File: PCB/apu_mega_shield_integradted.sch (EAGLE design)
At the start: 79 parts, among them IC1 74AHC573, IC10 DAC, IC11 IS62C1024AL, IC2 4050D, IC3 DS1307, IC4 LP298XS, IC5 S-SMP, IC6 S-DSP, IC7 LM2904, IC8 5x832 SRAM, IC9 5x832 SRAM, Q1 32.768, X1 MICROSDMOLEX

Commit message: R1 removed from PCB. It was supposed to be the current limiting resistor for the LCD backlight, however, the LCD module in use already has a current limiting resistor mounted right on that module.
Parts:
- removed R1: 220, resistor:R-US_R0805
- C10, C13: value (none) -> 100pF
- C11, C14: value (none) -> 1800pF
- C12, C9: value (none) -> 1000pF
- C15, C16, C17, C18, C19, C22, C23: value (none) -> 0.1uF
- C20, C21: value (none) -> 3pF
- C50, C51: value (none) -> 47uF
- DOWN: value (none) -> DOWN
- LEFT: value (none) -> LEFT
- R16, R17, R18, R19, R20, R21: value (none) -> 22K
- R22, R23: value (none) -> 5.1K
- RIGHT: value (none) -> RIGHT
- SELECT: value (none) -> SELECT
- UP: value (none) -> UP
- X2: value (none) -> 24.576Mhz
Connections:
- removed net !MUTE: IC6.!MUTE
- removed net SMPCLK: IC6.SMPCLK
- net N$14: now also U$6.46; no longer R1.2
- net VCC: no longer R1.1
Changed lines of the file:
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@@
 <part name="GND1" library="supply1" deviceset="GND" device=""/>
 <part name="JP1" library="pinhead" deviceset="PINHD-1X16" device="" value="LCD"/>
-<part name="UP" library="switch-omron" deviceset="10-XX" device=""/>
-<part name="DOWN" library="switch-omron" deviceset="10-XX" device=""/>
-<part name="LEFT" library="switch-omron" deviceset="10-XX" device=""/>
-<part name="RIGHT" library="switch-omron" deviceset="10-XX" device=""/>
-<part name="SELECT" library="switch-omron" deviceset="10-XX" device=""/>
+<part name="UP" library="switch-omron" deviceset="10-XX" device="" value="UP"/>
+<part name="DOWN" library="switch-omron" deviceset="10-XX" device="" value="DOWN"/>
+<part name="LEFT" library="switch-omron" deviceset="10-XX" device="" value="LEFT"/>
+<part name="RIGHT" library="switch-omron" deviceset="10-XX" device="" value="RIGHT"/>
+<part name="SELECT" library="switch-omron" deviceset="10-XX" device="" value="SELECT"/>
 <part name="Q1" library="crystal" deviceset="CRYTAL" device="SMD" value="32.768"/>
 <part name="IC3" library="adafruit" deviceset="DS1307" device="SMT" value="DS1307"/>
@@
 <part name="SUPPLY2" library="supply2" deviceset="GND" device=""/>
 <part name="X1" library="adafruit" deviceset="MICROSD" device="MOLEX"/>
-<part name="R1" library="resistor" deviceset="R-US_" device="R0805" value="220"/>
 <part name="R2" library="resistor" deviceset="R-US_" device="R0805" value="10K"/>
 <part name="R3" library="resistor" deviceset="R-US_" device="R0805" value="10K"/>
@@
 <part name="R15" library="resistor" deviceset="R-US_" device="R0805" value="10K"/>
 <part name="IC5" library="apu_pcb" deviceset="S-SMP" device=""/>
-<part name="C50" library="apu_pcb" deviceset="CAPACITOR" device=""/>
-<part name="C51" library="apu_pcb" deviceset="CAPACITOR" device=""/>
+<part name="C50" library="apu_pcb" deviceset="CAPACITOR" device="" value="47uF"/>
+<part name="C51" library="apu_pcb" deviceset="CAPACITOR" device="" value="47uF"/>
 <part name="IC6" library="apu_pcb" deviceset="S-DSP" device=""/>
 <part name="P+4" library="supply1" deviceset="VCC" device=""/>
 <part name="GND3" library="supply1" deviceset="GND" device=""/>
-<part name="C9" library="apu_pcb" deviceset="C0805" device=""/>
-<part name="C10" library="apu_pcb" deviceset="C0805" device=""/>
-<part name="C11" library="apu_pcb" deviceset="C0805" device=""/>
-<part name="C12" library="apu_pcb" deviceset="C0805" device=""/>
-<part name="C13" library="apu_pcb" deviceset="C0805" device=""/>
-<part name="C14" library="apu_pcb" deviceset="C0805" device=""/>
-<part name="C15" library="apu_pcb" deviceset="C0805" device=""/>
-<part name="C16" library="apu_pcb" deviceset="C0805" device=""/>
-<part name="C17" library="apu_pcb" deviceset="C0805" device=""/>
-<part name="C18" library="apu_pcb" deviceset="C0805" device=""/>
-<part name="C19" library="apu_pcb" deviceset="C0805" device=""/>
-<part name="C20" library="apu_pcb" deviceset="C0805" device=""/>
-<part name="C21" library="apu_pcb" deviceset="C0805" device=""/>
-<part name="R16" library="apu_pcb" deviceset="R0805" device=""/>
-<part name="R17" library="apu_pcb" deviceset="R0805" device=""/>
-<part name="R18" library="apu_pcb" deviceset="R0805" device=""/>
-<part name="R19" library="apu_pcb" deviceset="R0805" device=""/>
-<part name="R20" library="apu_pcb" deviceset="R0805" device=""/>
-<part name="R21" library="apu_pcb" deviceset="R0805" device=""/>
-<part name="R22" library="apu_pcb" deviceset="R0805" device=""/>
-<part name="R23" library="apu_pcb" deviceset="R0805" device=""/>
-<part name="C22" library="apu_pcb" deviceset="C0805" device=""/>
+<part name="C9" library="apu_pcb" deviceset="C0805" device="" value="1000pF"/>
+<part name="C10" library="apu_pcb" deviceset="C0805" device="" value="100pF"/>
+<part name="C11" library="apu_pcb" deviceset="C0805" device="" value="1800pF"/>
+<part name="C12" library="apu_pcb" deviceset="C0805" device="" value="1000pF"/>
+<part name="C13" library="apu_pcb" deviceset="C0805" device="" value="100pF"/>
+<part name="C14" library="apu_pcb" deviceset="C0805" device="" value="1800pF"/>
+<part name="C15" library="apu_pcb" deviceset="C0805" device="" value="0.1uF"/>
+<part name="C16" library="apu_pcb" deviceset="C0805" device="" value="0.1uF"/>
+<part name="C17" library="apu_pcb" deviceset="C0805" device="" value="0.1uF"/>
+<part name="C18" library="apu_pcb" deviceset="C0805" device="" value="0.1uF"/>
+<part name="C19" library="apu_pcb" deviceset="C0805" device="" value="0.1uF"/>
+<part name="C20" library="apu_pcb" deviceset="C0805" device="" value="3pF"/>
+<part name="C21" library="apu_pcb" deviceset="C0805" device="" value="3pF"/>
+<part name="R16" library="apu_pcb" deviceset="R0805" device="" value="22K"/>
+<part name="R17" library="apu_pcb" deviceset="R0805" device="" value="22K"/>
+<part name="R18" library="apu_pcb" deviceset="R0805" device="" value="22K"/>
+<part name="R19" library="apu_pcb" deviceset="R0805" device="" value="22K"/>
+<part name="R20" library="apu_pcb" deviceset="R0805" device="" value="22K"/>
+<part name="R21" library="apu_pcb" deviceset="R0805" device="" value="22K"/>
+<part name="R22" library="apu_pcb" deviceset="R0805" device="" value="5.1K"/>
+<part name="R23" library="apu_pcb" deviceset="R0805" device="" value="5.1K"/>
+<part name="C22" library="apu_pcb" deviceset="C0805" device="" value="0.1uF"/>
 <part name="GND5" library="supply1" deviceset="GND" device=""/>
 <part name="GND6" library="supply1" deviceset="GND" device=""/>
@@
 <part name="IC8" library="apu_pcb" deviceset="SRAM" device="" value="5x832 SRAM"/>
 <part name="IC9" library="apu_pcb" deviceset="SRAM" device="" value="5x832 SRAM"/>
-<part name="X2" library="apu_pcb" deviceset="CRYSTAL" device=""/>
+<part name="X2" library="apu_pcb" deviceset="CRYSTAL" device="" value="24.576Mhz"/>
 <part name="IC10" library="apu_pcb" deviceset="UPD6376" device="" value="DAC"/>
-<part name="C23" library="apu_pcb" deviceset="C0805" device=""/>
+<part name="C23" library="apu_pcb" deviceset="C0805" device="" value="0.1uF"/>
 <part name="C24" library="rcl" deviceset="C-EU" device="C0805" value="0.1uF"/>
 <part name="P+5" library="supply1" deviceset="VCC" device=""/>
@@
 <instance part="UP" gate="1" x="147.32" y="-17.78" smashed="yes" rot="MR270">
 <attribute name="NAME" x="148.844" y="-22.606" size="1.778" layer="95" rot="MR0"/>
-<attribute name="VALUE" x="144.145" y="-13.97" size="1.778" layer="96" rot="MR0"/>
 </instance>
 <instance part="DOWN" gate="1" x="147.32" y="-30.48" smashed="yes" rot="MR270">
 <attribute name="NAME" x="150.876" y="-35.56" size="1.778" layer="95" rot="MR0"/>
-<attribute name="VALUE" x="144.145" y="-26.67" size="1.778" layer="96" rot="MR0"/>
 </instance>
 <instance part="LEFT" gate="1" x="132.08" y="-22.86" smashed="yes" rot="MR270">
 <attribute name="NAME" x="135.128" y="-27.94" size="1.778" layer="95" rot="MR0"/>
-<attribute name="VALUE" x="128.905" y="-19.05" size="1.778" layer="96" rot="MR0"/>
 </instance>
 <instance part="RIGHT" gate="1" x="165.1" y="-22.86" smashed="yes" rot="MR270">
 <attribute name="NAME" x="169.164" y="-27.686" size="1.778" layer="95" rot="MR0"/>
-<attribute name="VALUE" x="161.925" y="-19.05" size="1.778" layer="96" rot="MR0"/>
 </instance>
 <instance part="SELECT" gate="1" x="182.88" y="-22.86" smashed="yes" rot="MR270">
 <attribute name="NAME" x="187.198" y="-27.686" size="1.778" layer="95" rot="MR0"/>
-<attribute name="VALUE" x="179.705" y="-19.05" size="1.778" layer="96" rot="MR0"/>
 </instance>
 <instance part="Q1" gate="G$1" x="111.76" y="127" rot="R180"/>
@@
 <instance part="SUPPLY2" gate="GND" x="383.54" y="-15.24"/>
 <instance part="X1" gate="G$1" x="353.06" y="15.24"/>
-<instance part="R1" gate="G$1" x="233.68" y="121.92" rot="R270"/>
 <instance part="R2" gate="G$1" x="142.24" y="5.08" rot="R270"/>
 <instance part="R3" gate="G$1" x="182.88" y="5.08" rot="R270"/>
@@
 <wire x1="243.84" y1="114.3" x2="243.84" y2="116.84" width="0.1524" layer="91"/>
 <label x="256.54" y="134.62" size="1.778" layer="95"/>
-<pinref part="R1" gate="G$1" pin="1"/>
-<wire x1="233.68" y1="127" x2="243.84" y2="127" width="0.1524" layer="91"/>
-<junction x="243.84" y="127"/>
 </segment>
 <segment>
@@
 <segment>
 <pinref part="JP1" gate="A" pin="15"/>
-<pinref part="R1" gate="G$1" pin="2"/>
 <wire x1="233.68" y1="111.76" x2="233.68" y2="116.84" width="0.1524" layer="91"/>
+<wire x1="233.68" y1="116.84" x2="251.46" y2="116.84" width="0.1524" layer="91"/>
+<wire x1="251.46" y1="116.84" x2="251.46" y2="101.6" width="0.1524" layer="91"/>
+<pinref part="U$6" gate="G$1" pin="46"/>
+<wire x1="251.46" y1="101.6" x2="259.08" y2="101.6" width="0.1524" layer="91"/>
 </segment>
 </net>
@@
 </instances>
 <busses>
-<bus name="PA[0..7],PD[0..7],!P_RD,!P_WR,!RESET,!MUTE,SMPCLK,LEFT,RIGHT,GND,VCC,XTAL1,XTAL2,A[0..14],D[0..7],!CE0,!CE1,!OE,!WE,L.OUT,R.OUT,BCK,LRCK,SO,AVCC">
+<bus name="PA[0..7],PD[0..7],!RD,!WR,RST,!MUTE,SMPCLK,LEFT,RIGHT,GND,VCC,XTAL1,XTAL2,A[0..32],D[0..15],!CE0,!CE1,!OE,!WE,L.OUT,R.OUT,BCK,LRCK,SO,AVCC">
 <segment>
 <wire x1="134.62" y1="60.96" x2="134.62" y2="12.7" width="0.762" layer="92"/>
@@
 </segment>
 </net>
-<net name="SMPCLK" class="0">
-<segment>
-<pinref part="IC6" gate="G$1" pin="SMPCLK"/>
-<wire x1="139.7" y1="55.88" x2="134.62" y2="55.88" width="0.1524" layer="91"/>
-</segment>
-</net>
-<net name="!MUTE" class="1">
-<segment>
-<pinref part="IC6" gate="G$1" pin="!MUTE"/>
-<wire x1="139.7" y1="58.42" x2="134.62" y2="58.42" width="0.1524" layer="91"/>
-</segment>
-</net>

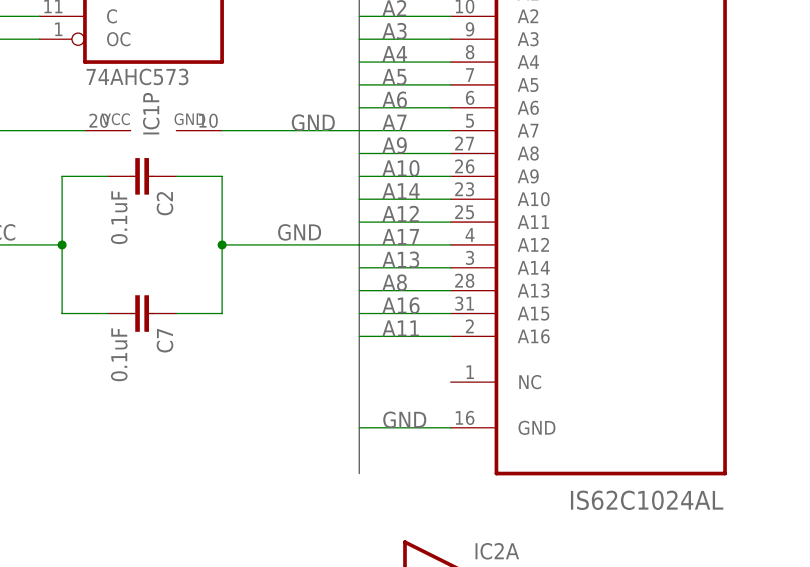
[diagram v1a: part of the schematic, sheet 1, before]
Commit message: Optimized layout a bit more.
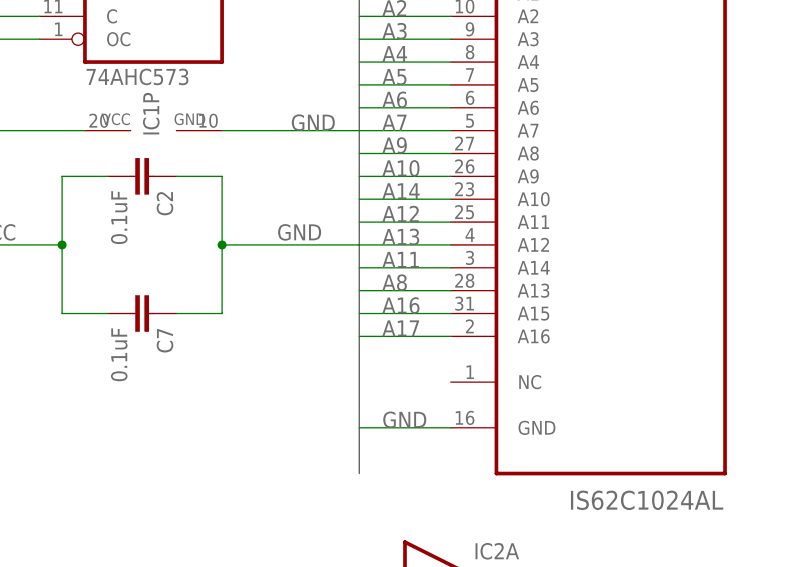
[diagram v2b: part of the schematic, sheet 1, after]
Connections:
- net A11: now also IC11.A14; no longer IC11.A16
- net A13: now also IC11.A12; no longer IC11.A14
- net A17: now also IC11.A16; no longer IC11.A12
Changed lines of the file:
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@@
 <net name="A11" class="0">
-<segment>
-<pinref part="IC11" gate="A" pin="A16"/>
-<wire x1="355.6" y1="78.74" x2="345.44" y2="78.74" width="0.1524" layer="91"/>
-<label x="347.98" y="78.74" size="1.778" layer="95"/>
-</segment>
 <segment>
 <pinref part="U$6" gate="G$1" pin="34"/>
 <wire x1="261.62" y1="116.84" x2="259.08" y2="116.84" width="0.1524" layer="91"/>
 <label x="256.54" y="116.84" size="1.778" layer="95"/>
+</segment>
+<segment>
+<pinref part="IC11" gate="A" pin="A14"/>
+<wire x1="355.6" y1="86.36" x2="345.44" y2="86.36" width="0.1524" layer="91"/>
+<label x="347.98" y="86.36" size="1.778" layer="95"/>
 </segment>
 </net>
@@
 <net name="A13" class="0">
 <segment>
-<pinref part="IC11" gate="A" pin="A14"/>
-<wire x1="355.6" y1="86.36" x2="345.44" y2="86.36" width="0.1524" layer="91"/>
-<label x="347.98" y="86.36" size="1.778" layer="95"/>
-</segment>
-<segment>
 <pinref part="U$6" gate="G$1" pin="32"/>
 <wire x1="261.62" y1="119.38" x2="259.08" y2="119.38" width="0.1524" layer="91"/>
 <label x="256.54" y="119.38" size="1.778" layer="95"/>
+</segment>
+<segment>
+<pinref part="IC11" gate="A" pin="A12"/>
+<wire x1="355.6" y1="88.9" x2="345.44" y2="88.9" width="0.1524" layer="91"/>
+<label x="347.98" y="88.9" size="1.778" layer="95"/>
 </segment>
 </net>
@@
 </segment>
 <segment>
-<pinref part="IC11" gate="A" pin="A12"/>
-<wire x1="345.44" y1="88.9" x2="355.6" y2="88.9" width="0.1524" layer="91"/>
-<label x="347.98" y="88.9" size="1.778" layer="95"/>
+<pinref part="IC11" gate="A" pin="A16"/>
+<wire x1="355.6" y1="78.74" x2="345.44" y2="78.74" width="0.1524" layer="91"/>
+<label x="347.98" y="78.74" size="1.778" layer="95"/>
 </segment>
 </net>

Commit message: Final revisions to the PCB design, hopefully. :)
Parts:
- C1, C2, C24, C7: device rcl:C-EUC0805 -> apu_pcb:C0805
- C3, C4, C5, C6: device resistor:C-EUC0805 -> apu_pcb:C0805
- R10, R11, R12, R13, R14, R15, R2, R3, R4, R5, R7, R8, R9: device resistor:R-US_R0805 -> adafruit:R-US_R0805
- R16, R17, R18, R19, R20, R21, R22, R23: device apu_pcb:R0805 -> adafruit:R-US_R0805
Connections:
- net N$14 renamed PWM
- net ALEFT: now also C14.2, R23.1; no longer C14.P$2, R23.P$1
- net ARIGHT: now also C11.2, R22.1; no longer C11.P$2, R22.P$1
- net GND: now also C10.1, C12.2, C13.1, C15.2, C16.2, C17.2, C18.2, C19.2, C20.1, C21.1, C22.1, C23.2, C9.1, R22.2, R23.2, U$4.P$4, U$5.P$4; no longer C10.P$1, C12.P$2, C13.P$1, C15.P$2, C16.P$2, C17.P$2, C18.P$2, C19.P$2, C20.P$1, C21.P$1, C22.P$1, C23.P$2, C9.P$1, R22.P$2, R23.P$2, U$4.PGND1, U$5.PGND1
- net L.OUT: now also R16.2; no longer R16.P$2
- net L1: now also C12.1, R19.2, R20.2; no longer C12.P$1, R19.P$2, R20.P$2
- net L2: now also C14.1, R19.1, R21.2; no longer C14.P$1, R19.P$1, R21.P$2
- net L3: now also C13.2, R21.1; no longer C13.P$2, R21.P$1
- net N$2: now also U$4.P$1; no longer U$4.PSIG
- net N$3: now also U$5.P$1; no longer U$5.PSIG
- net R.OUT: now also R20.1; no longer R20.P$1
- net R1: now also C9.2, R16.1, R17.2; no longer C9.P$2, R16.P$1, R17.P$2
- net R2: now also C11.1, R17.1, R18.2; no longer C11.P$1, R17.P$1, R18.P$2
- net R3: now also C10.2, R18.1; no longer C10.P$2, R18.P$1
- net VCC: now also C15.1, C16.1, C17.1, C18.1, C19.1, C22.2, C23.1; no longer C15.P$1, C16.P$1, C17.P$1, C18.P$1, C19.P$1, C22.P$2, C23.P$1
- net XTAL1: now also C21.2; no longer C21.P$2
- net XTAL2: now also C20.2; no longer C20.P$2
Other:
- moved on the sheet: C1, C2, C24, C3, C4, C5, C6, C7
